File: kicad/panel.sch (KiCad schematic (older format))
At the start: 7 parts, among them CON21 Panel1, CON22 Panel2, SW1 SW_PUSH, U2 SN74HCT245PW

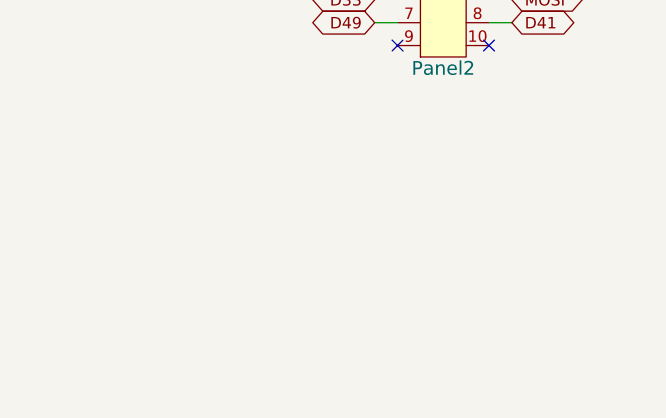
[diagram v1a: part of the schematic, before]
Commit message: Add AUX connectro for a few buttons or so
close #14
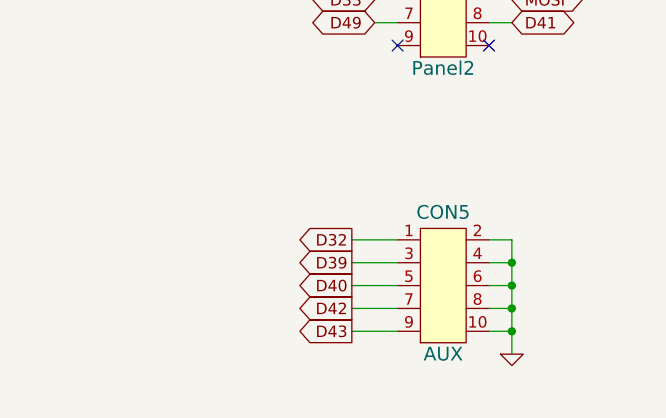
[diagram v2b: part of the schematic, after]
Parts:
- added CON5: AUX, symbol CON5x2
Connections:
- net GND: now also CON5.10, CON5.2, CON5.4, CON5.6, CON5.8
- new net D32: CON5.1
- new net D39: CON5.3
- new net D40: CON5.5
- new net D42: CON5.7
- new net D43: CON5.9
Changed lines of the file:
@@
 D13
 $Comp
-L GND #PWR064
+L GND #PWR51
 U 1 1 534EE36C
 P 2000 2250
-F 0 "#PWR064" H 2000 2250 30  0001 C CNN
+F 0 "#PWR51" H 2000 2250 30  0001 C CNN
 F 1 "GND" H 2000 2180 30  0001 C CNN
 F 2 "~" H 2000 2250 60  0000 C CNN
@@
 $EndComp
 $Comp
-L GND #PWR065
+L GND #PWR50
 U 1 1 536AA50B
 P 2950 2150
-F 0 "#PWR065" H 2950 2150 30  0001 C CNN
+F 0 "#PWR50" H 2950 2150 30  0001 C CNN
 F 1 "GND" H 2950 2080 30  0001 C CNN
 F 2 "~" H 2950 2150 60  0000 C CNN
@@
 	5650 1500 5250 1500
 $Comp
-L GND #PWR066
+L GND #PWR49
 U 1 1 538CDD99
 P 5550 2000
-F 0 "#PWR066" H 5550 2000 30  0001 C CNN
+F 0 "#PWR49" H 5550 2000 30  0001 C CNN
 F 1 "GND" H 5550 1930 30  0001 C CNN
 F 2 "~" H 5550 2000 60  0000 C CNN
@@
 $EndComp
 $Comp
-L GND #PWR067
+L GND #PWR55
 U 1 1 538E32BE
 P 3450 4350
-F 0 "#PWR067" H 3450 4350 30  0001 C CNN
+F 0 "#PWR55" H 3450 4350 30  0001 C CNN
 F 1 "GND" H 3450 4280 30  0001 C CNN
 F 2 "" H 3450 4350 60  0000 C CNN
@@
 	3200 3950 3650 3950
 $Comp
-L GND #PWR068
+L GND #PWR54
 U 1 1 538E3349
 P 3250 4350
-F 0 "#PWR068" H 3250 4350 30  0001 C CNN
+F 0 "#PWR54" H 3250 4350 30  0001 C CNN
 F 1 "GND" H 3250 4280 30  0001 C CNN
 F 2 "" H 3250 4350 60  0000 C CNN
@@
 	2500 4050 2300 4050
 $Comp
-L GND #PWR069
+L GND #PWR53
 U 1 1 538E301C
 P 2400 4350
-F 0 "#PWR069" H 2400 4350 30  0001 C CNN
+F 0 "#PWR53" H 2400 4350 30  0001 C CNN
 F 1 "GND" H 2400 4280 30  0001 C CNN
 F 2 "" H 2400 4350 60  0000 C CNN
@@
 NoConn ~ 3200 3650
 NoConn ~ 3200 3750
+$Comp
+L CON5x2 CON5
+U 1 1 53946F92
+P 5850 3900
+F 0 "CON5" H 5850 4220 60  0000 C CNN
+F 1 "AUX" H 5850 3600 60  0000 C CNN
+F 2 "" H 5850 3900 40  0000 C CNN
+F 3 "" H 5850 3900 40  0000 C CNN
+	1    5850 3900
+	1    0    0    -1
+$EndComp
+Text GLabel 5450 3700 0    50   Output ~ 0
+D32
+Text GLabel 5450 3800 0    50   Output ~ 0
+D39
+Text GLabel 5450 3900 0    50   Output ~ 0
+D40
+Text GLabel 5450 4000 0    50   Output ~ 0
+D42
+Text GLabel 5450 4100 0    50   Output ~ 0
+D43
+Wire Wire Line
+	5450 3700 5650 3700
+Wire Wire Line
+	5650 3800 5450 3800
+Wire Wire Line
+	5450 3900 5650 3900
+Wire Wire Line
+	5650 4000 5450 4000
+Wire Wire Line
+	5450 4100 5650 4100
+Wire Wire Line
+	6050 3700 6150 3700
+Wire Wire Line
+	6150 3700 6150 4200
+Wire Wire Line
+	6050 4100 6150 4100
+Connection ~ 6150 4100
+Wire Wire Line
+	6050 4000 6150 4000
+Connection ~ 6150 4000
+Wire Wire Line
+	6050 3900 6150 3900
+Connection ~ 6150 3900
+Wire Wire Line
+	6050 3800 6150 3800
+Connection ~ 6150 3800
+$Comp
+L GND #PWR52
+U 1 1 539474AA
+P 6150 4200
+F 0 "#PWR52" H 6150 4200 30  0001 C CNN
+F 1 "GND" H 6150 4130 30  0001 C CNN
+F 2 "" H 6150 4200 60  0000 C CNN
+F 3 "" H 6150 4200 60  0000 C CNN
+	1    6150 4200
+	1    0    0    -1
+$EndComp
 $EndSCHEMATC

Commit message: Add footprint informations
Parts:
- CON21, CON22, CON5: footprint (none) -> IDC10
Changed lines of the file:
@@
 F 0 "CON21" H 5850 2020 60  0000 C CNN
 F 1 "Panel1" H 5850 1400 60  0000 C CNN
-F 2 "" H 5850 1700 40  0000 C CNN
+F 2 "IDC10" H 5850 1700 40  0000 C CNN
 F 3 "" H 5850 1700 40  0000 C CNN
 	1    5850 1700
@@
 F 0 "CON22" H 5850 2970 60  0000 C CNN
 F 1 "Panel2" H 5850 2350 60  0000 C CNN
-F 2 "" H 5850 2650 40  0000 C CNN
+F 2 "IDC10" H 5850 2650 40  0000 C CNN
 F 3 "" H 5850 2650 40  0000 C CNN
 	1    5850 2650
@@
 F 0 "CON5" H 5850 4220 60  0000 C CNN
 F 1 "AUX" H 5850 3600 60  0000 C CNN
-F 2 "" H 5850 3900 40  0000 C CNN
+F 2 "IDC10" H 5850 3900 40  0000 C CNN
 F 3 "" H 5850 3900 40  0000 C CNN
 	1    5850 3900

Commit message: Add footprint informations
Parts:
- D15: footprint 0805 -> 0805D
- U2: footprint (none) -> TSSOP20
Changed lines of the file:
@@
 D13
 $Comp
-L GND #PWR049
+L GND #PWR51
 U 1 1 534EE36C
 P 2000 2250
-F 0 "#PWR049" H 2000 2250 30  0001 C CNN
+F 0 "#PWR51" H 2000 2250 30  0001 C CNN
 F 1 "GND" H 2000 2180 30  0001 C CNN
 F 2 "~" H 2000 2250 60  0000 C CNN
@@
 $EndComp
 $Comp
-L GND #PWR050
+L GND #PWR50
 U 1 1 536AA50B
 P 2950 2150
-F 0 "#PWR050" H 2950 2150 30  0001 C CNN
+F 0 "#PWR50" H 2950 2150 30  0001 C CNN
 F 1 "GND" H 2950 2080 30  0001 C CNN
 F 2 "~" H 2950 2150 60  0000 C CNN
@@
 F 0 "D15" H 2000 2050 60  0000 C CNN
 F 1 "GREEN" H 2000 1850 60  0000 C CNN
-F 2 "0805" H 2000 1785 40  0000 C CNN
+F 2 "0805D" H 2000 1785 40  0000 C CNN
 F 3 "~" H 2000 1950 60  0000 C CNN
 	1    2000 1950
@@
 	5650 1500 5250 1500
 $Comp
-L GND #PWR051
+L GND #PWR49
 U 1 1 538CDD99
 P 5550 2000
-F 0 "#PWR051" H 5550 2000 30  0001 C CNN
+F 0 "#PWR49" H 5550 2000 30  0001 C CNN
 F 1 "GND" H 5550 1930 30  0001 C CNN
 F 2 "~" H 5550 2000 60  0000 C CNN
@@
 F 0 "U2" H 2850 3950 60  0000 C CNN
 F 1 "SN74HCT245PW" H 2850 3850 60  0000 C CNN
-F 2 "" H 2850 3900 60  0000 C CNN
+F 2 "TSSOP20" H 2850 2550 40  0000 C CNN
 F 3 "" H 2850 3900 60  0000 C CNN
 	1    2850 3400
@@
 $EndComp
 $Comp
-L GND #PWR052
+L GND #PWR55
 U 1 1 538E32BE
 P 3450 4350
-F 0 "#PWR052" H 3450 4350 30  0001 C CNN
+F 0 "#PWR55" H 3450 4350 30  0001 C CNN
 F 1 "GND" H 3450 4280 30  0001 C CNN
 F 2 "" H 3450 4350 60  0000 C CNN
@@
 	3200 3950 3650 3950
 $Comp
-L GND #PWR053
+L GND #PWR54
 U 1 1 538E3349
 P 3250 4350
-F 0 "#PWR053" H 3250 4350 30  0001 C CNN
+F 0 "#PWR54" H 3250 4350 30  0001 C CNN
 F 1 "GND" H 3250 4280 30  0001 C CNN
 F 2 "" H 3250 4350 60  0000 C CNN
@@
 	2500 4050 2300 4050
 $Comp
-L GND #PWR054
+L GND #PWR53
 U 1 1 538E301C
 P 2400 4350
-F 0 "#PWR054" H 2400 4350 30  0001 C CNN
+F 0 "#PWR53" H 2400 4350 30  0001 C CNN
 F 1 "GND" H 2400 4280 30  0001 C CNN
 F 2 "" H 2400 4350 60  0000 C CNN
@@
 Connection ~ 6150 3800
 $Comp
-L GND #PWR055
+L GND #PWR52
 U 1 1 539474AA
 P 6150 4200
-F 0 "#PWR055" H 6150 4200 30  0001 C CNN
+F 0 "#PWR52" H 6150 4200 30  0001 C CNN
 F 1 "GND" H 6150 4130 30  0001 C CNN
 F 2 "" H 6150 4200 60  0000 C CNN

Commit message: Place arduino shield connectors
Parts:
- SW1: footprint (none) -> PIN2
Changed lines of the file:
@@
 F 0 "SW1" H 3100 1860 50  0000 C CNN
 F 1 "SW_PUSH" H 2950 1670 50  0000 C CNN
-F 2 "" H 2950 1750 60  0000 C CNN
+F 2 "PIN2" H 2950 1600 40  0000 C CNN
 F 3 "" H 2950 1750 60  0000 C CNN
 	1    2950 1750
